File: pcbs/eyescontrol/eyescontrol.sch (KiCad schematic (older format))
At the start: 13 parts, among them IC1 ATMEGA88-P, P1 EYES, P2 PROG_MICRO, P3 CONN_01X04, SW1 SW_PUSH, Y1 18.432 MHz

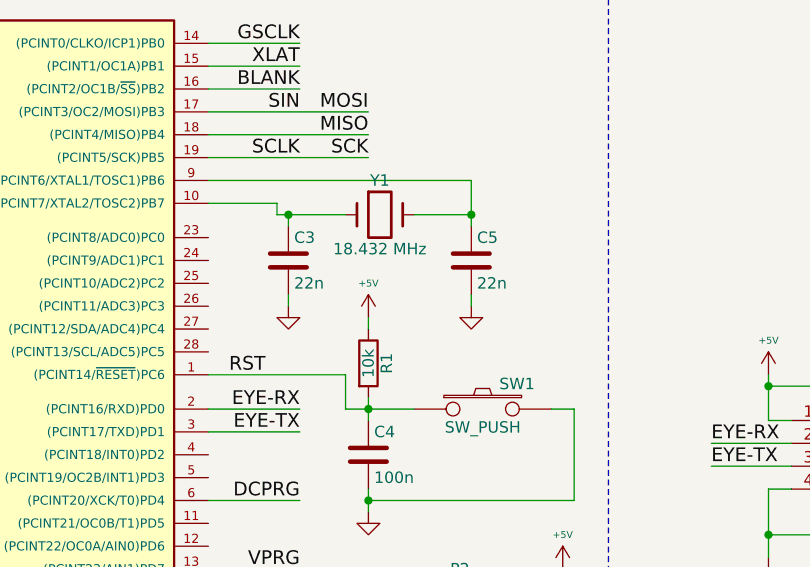
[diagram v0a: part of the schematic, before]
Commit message: primera version del pcb de la placa principal, falta verificar footprints
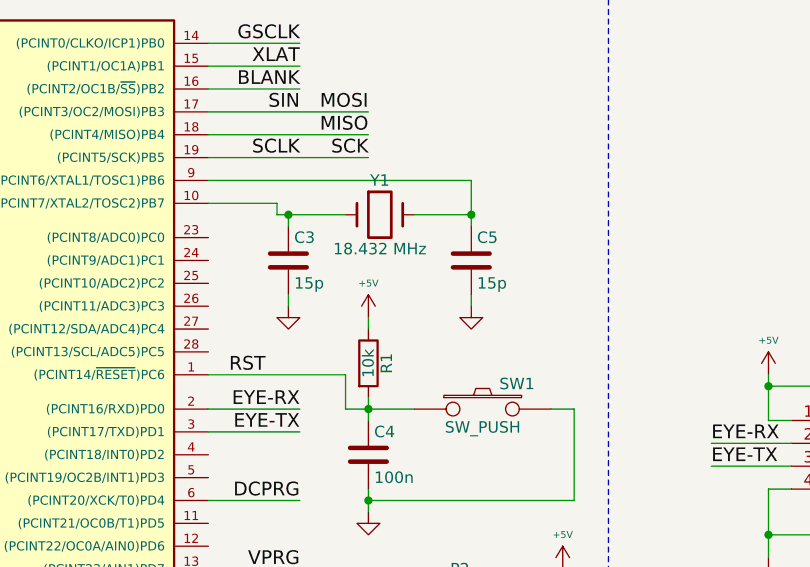
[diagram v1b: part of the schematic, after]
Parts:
- C3, C5: value 22n -> 15p
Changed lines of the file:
@@
 P 5500 2350
 F 0 "C5" H 5525 2450 50  0000 L CNN
-F 1 "22n" H 5525 2250 50  0000 L CNN
+F 1 "15p" H 5525 2250 50  0000 L CNN
 F 2 "Capacitors_ThroughHole:C_Rect_L4_W2.5_P2.5" H 5538 2200 30  0001 C CNN
 F 3 "" H 5500 2350 60  0000 C CNN
@@
 P 4700 2350
 F 0 "C3" H 4725 2450 50  0000 L CNN
-F 1 "22n" H 4725 2250 50  0000 L CNN
+F 1 "15p" H 4725 2250 50  0000 L CNN
 F 2 "Capacitors_ThroughHole:C_Rect_L4_W2.5_P2.5" H 4738 2200 30  0001 C CNN
 F 3 "" H 4700 2350 60  0000 C CNN

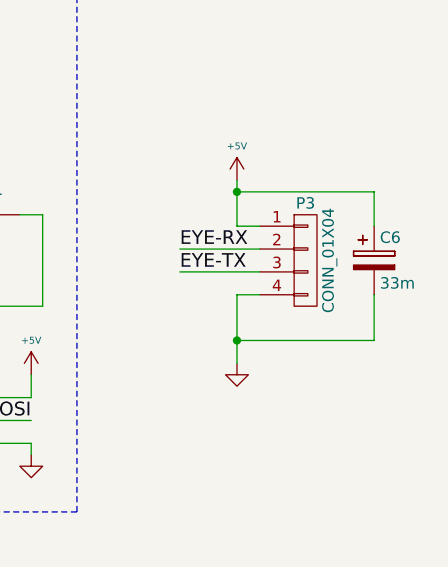
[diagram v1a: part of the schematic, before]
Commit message: actualizo las 3 placas, revisar y mandar a fabricar
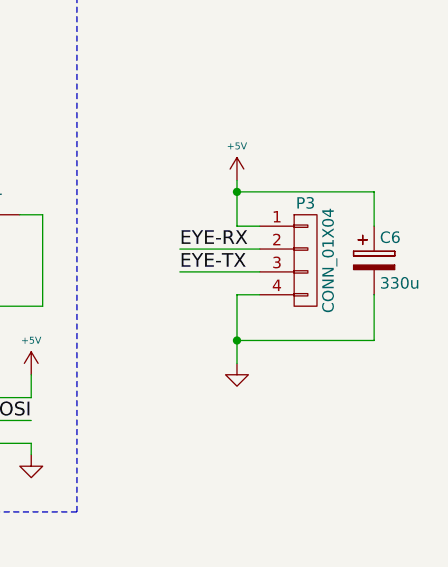
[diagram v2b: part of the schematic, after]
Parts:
- C6: value 33m -> 330u; footprint Capacitors_ThroughHole:C_Radial_D8_L13_P3.8 -> Capacitors_ThroughHole:C_Radial_D8_L11.5_P3.5
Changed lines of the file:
@@
 P 7400 3200
 F 0 "C6" H 7425 3300 50  0000 L CNN
-F 1 "33m" H 7425 3100 50  0000 L CNN
-F 2 "Capacitors_ThroughHole:C_Radial_D8_L13_P3.8" H 7438 3050 30  0001 C CNN
+F 1 "330u" H 7425 3100 50  0000 L CNN
+F 2 "Capacitors_ThroughHole:C_Radial_D8_L11.5_P3.5" H 7438 3050 30  0001 C CNN
 F 3 "" H 7400 3200 60  0000 C CNN
 	1    7400 3200
